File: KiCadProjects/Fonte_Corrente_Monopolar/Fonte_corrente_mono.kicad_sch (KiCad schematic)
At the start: 24 parts, among them J1 Vref, J2 tensoes, J3 sinais analogicos, J4 comunicacao / sinais digitais, J5 Vref, J6 Pinos de verificação, U1 AD828AN, U2 INA128, U3 AD828AN

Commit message: autosave backup
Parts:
- J1, J5: footprint (none) -> Connector_PinHeader_2.54mm:PinHeader_1x03_P2.54mm_Vertical
- U1, U3: footprint AD828:N_8_ADI -> AD828AN:N_8_ADI
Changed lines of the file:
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@@
       (effects (font (size 1.27 1.27)) (justify right))
     )
-    (property "Footprint" "" (at 229.87 95.885 0)
+    (property "Footprint" "Connector_PinHeader_2.54mm:PinHeader_1x03_P2.54mm_Vertical" (at 229.87 95.885 0)
       (effects (font (size 1.27 1.27)) hide)
     )
@@
       (effects (font (size 1.524 1.524)))
     )
-    (property "Footprint" "AD828:N_8_ADI" (at 118.745 116.84 0)
+    (property "Footprint" "AD828AN:N_8_ADI" (at 118.745 116.84 0)
       (effects (font (size 1.27 1.27) italic) hide)
     )
@@
       (effects (font (size 1.27 1.27)) (justify right))
     )
-    (property "Footprint" "" (at 177.8 95.885 0)
+    (property "Footprint" "Connector_PinHeader_2.54mm:PinHeader_1x03_P2.54mm_Vertical" (at 177.8 95.885 0)
       (effects (font (size 1.27 1.27)) hide)
     )
@@
       (effects (font (size 1.524 1.524)))
     )
-    (property "Footprint" "AD828:N_8_ADI" (at 58.674 33.274 0)
+    (property "Footprint" "AD828AN:N_8_ADI" (at 58.674 33.274 0)
       (effects (font (size 1.27 1.27) italic) hide)
     )

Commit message: alterações PCB
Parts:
- renumbered Rg1 to RganhoINA1, Rs1 to Rsentinela1
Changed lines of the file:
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@@
   (symbol (lib_id "Device:R") (at 195.58 45.72 0) (unit 1)
     (in_bom yes) (on_board yes) (dnp no) (fields_autoplaced)
-    (property "Reference" "Rg1" (at 198.12 45.085 0)
+    (property "Reference" "RganhoINA1" (at 198.12 44.45 0)
       (effects (font (size 1.27 1.27)) (justify left))
     )
-    (property "Value" "3,3k" (at 198.12 47.625 0)
+    (property "Value" "3,3k" (at 198.12 46.99 0)
       (effects (font (size 1.27 1.27)) (justify left))
     )
@@
       (project "Fonte_corrente_mono"
         (path "/f0ff92cf-26e5-4ab9-977d-5f9689e8a5d0"
-          (reference "Rg1") (unit 1)
+          (reference "RganhoINA1") (unit 1)
         )
       )
@@
   (symbol (lib_id "Device:R") (at 183.515 45.72 0) (unit 1)
     (in_bom yes) (on_board yes) (dnp no) (fields_autoplaced)
-    (property "Reference" "Rs1" (at 185.42 45.085 0)
+    (property "Reference" "Rsentinela1" (at 185.42 44.45 0)
       (effects (font (size 1.27 1.27)) (justify left))
     )
-    (property "Value" "10" (at 185.42 47.625 0)
+    (property "Value" "10" (at 185.42 46.99 0)
       (effects (font (size 1.27 1.27)) (justify left))
     )
@@
       (project "Fonte_corrente_mono"
         (path "/f0ff92cf-26e5-4ab9-977d-5f9689e8a5d0"
-          (reference "Rs1") (unit 1)
+          (reference "Rsentinela1") (unit 1)
         )
       )

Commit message: autosave backup
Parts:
- added SW_kcd1: sw, Chave_Gangorra:chave gangorra 3 pinos, symbol chave_gangorra_kcd1_2pinos:chave_gangorra_
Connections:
- net Sin1: now also SW_kcd1. (1a)
- net SinA: now also SW_kcd1. (1a)
- net switch_out_1: no longer names the net of U1.3 (+IN1)
- net switch_out_1: now also SW_kcd1. (1a)

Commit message: alterações PCB
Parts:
- removed J6: Pinos de verificação, Connector_PinHeader_2.54mm:PinHeader_1x14_P2.54mm_Horizontal, symbol Connector_Generic:Conn_01x14
- removed SW_kcd1: sw, Chave_Gangorra:chave gangorra 3 pinos, symbol chave_gangorra_kcd1_2pinos:chave_gangorra_
- added SW_kcd1: sw, Chave_Gangorra:chave gangorra 3 pinos, symbol chave_gangorra_kcd1:chave_gangorra_
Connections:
- net Sin1: now also SW_kcd1.2 (1a)
- net SinA: now also SW_kcd1.3 (1b)
- net at U1.3 (+IN1): now also SW_kcd1.1

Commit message: alterações PCB
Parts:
- renumbered U1 to U1-howland1, U3 to U3-cond1
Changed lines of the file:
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@@
   (symbol (lib_id "AD828AN:AD828AN") (at 118.745 116.84 0) (unit 1)
     (in_bom yes) (on_board yes) (dnp no) (fields_autoplaced)
-    (property "Reference" "U3" (at 139.065 107.95 0)
+    (property "Reference" "U3-cond1" (at 139.065 106.68 0)
       (effects (font (size 1.524 1.524)))
     )
-    (property "Value" "AD828AN" (at 139.065 110.49 0)
+    (property "Value" "AD828AN" (at 139.065 109.22 0)
       (effects (font (size 1.524 1.524)))
     )
@@
       (project "Fonte_corrente_mono"
         (path "/f0ff92cf-26e5-4ab9-977d-5f9689e8a5d0"
-          (reference "U3") (unit 1)
+          (reference "U3-cond1") (unit 1)
         )
       )
@@
   (symbol (lib_id "2023-04-18_19-29-20:AD828AN") (at 58.42 33.02 0) (unit 1)
     (in_bom yes) (on_board yes) (dnp no) (fields_autoplaced)
-    (property "Reference" "U1" (at 78.74 24.13 0)
+    (property "Reference" "U1-howland1" (at 78.74 22.86 0)
       (effects (font (size 1.524 1.524)))
     )
-    (property "Value" "AD828AN" (at 78.74 26.67 0)
+    (property "Value" "AD828AN" (at 78.74 25.4 0)
       (effects (font (size 1.524 1.524)))
     )
@@
       (project "Fonte_corrente_mono"
         (path "/f0ff92cf-26e5-4ab9-977d-5f9689e8a5d0"
-          (reference "U1") (unit 1)
-        )
-      )
+          (reference "U1-howland1") (unit 1)
+        )
+      )

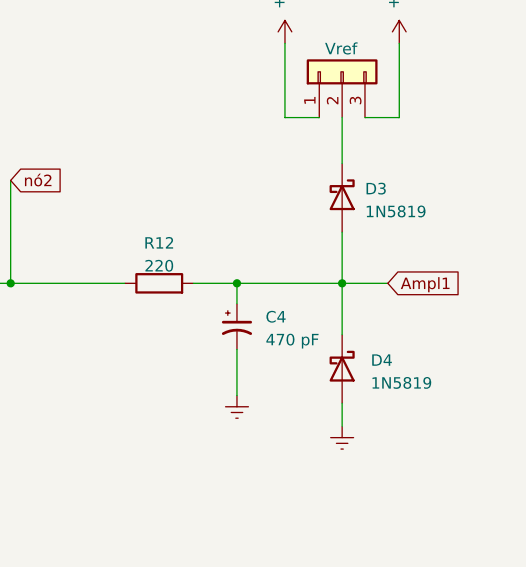
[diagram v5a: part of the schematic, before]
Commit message: alterações PCB: tamanho de pad
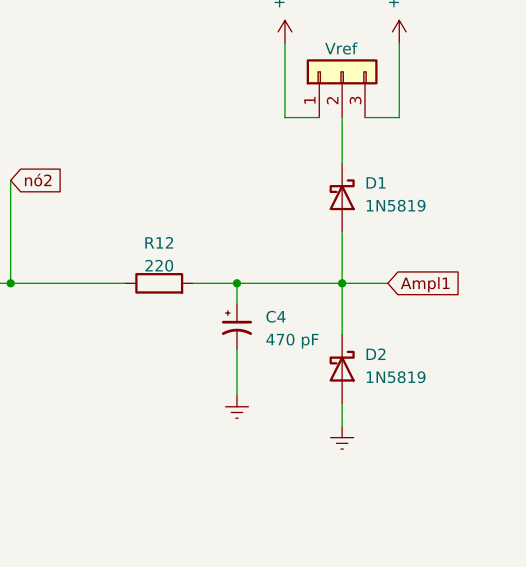
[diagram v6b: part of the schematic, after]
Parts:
- renumbered D3 to D1, D4 to D2
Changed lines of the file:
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@@
   (symbol (lib_id "Diode:1N5819") (at 229.87 109.855 270) (unit 1)
     (in_bom yes) (on_board yes) (dnp no) (fields_autoplaced)
-    (property "Reference" "D3" (at 232.41 108.9025 90)
+    (property "Reference" "D1" (at 232.41 108.2675 90)
       (effects (font (size 1.27 1.27)) (justify left))
     )
-    (property "Value" "1N5819" (at 232.41 111.4425 90)
+    (property "Value" "1N5819" (at 232.41 110.8075 90)
       (effects (font (size 1.27 1.27)) (justify left))
     )
@@
       (project "Fonte_corrente_mono"
         (path "/f0ff92cf-26e5-4ab9-977d-5f9689e8a5d0"
-          (reference "D3") (unit 1)
+          (reference "D1") (unit 1)
         )
       )
@@
   (symbol (lib_id "Diode:1N5819") (at 229.87 128.905 270) (unit 1)
     (in_bom yes) (on_board yes) (dnp no) (fields_autoplaced)
-    (property "Reference" "D4" (at 233.045 127.9525 90)
+    (property "Reference" "D2" (at 232.41 127.3175 90)
       (effects (font (size 1.27 1.27)) (justify left))
     )
-    (property "Value" "1N5819" (at 233.045 130.4925 90)
+    (property "Value" "1N5819" (at 232.41 129.8575 90)
       (effects (font (size 1.27 1.27)) (justify left))
     )
@@
       (project "Fonte_corrente_mono"
         (path "/f0ff92cf-26e5-4ab9-977d-5f9689e8a5d0"
-          (reference "D4") (unit 1)
+          (reference "D2") (unit 1)
         )
       )

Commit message: alterações PCB
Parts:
- removed J5: Vref, Connector_PinHeader_2.54mm:PinHeader_1x03_P2.54mm_Vertical, symbol Connector_Generic:Conn_01x03
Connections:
- net at D1.1 (K): now also J1.2 (Pin_2), R10.1
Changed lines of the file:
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@@
   (junction (at 159.385 119.38) (diameter 0) (color 0 0 0 0)
   )
+  (junction (at 177.8 102.87) (diameter 0) (color 0 0 0 0)
+  )
   (junction (at 177.8 119.38) (diameter 0) (color 0 0 0 0)
   )
@@
   (junction (at 108.585 35.56) (diameter 0) (color 0 0 0 0)
   )
-  (wire (pts (xy 227.33 100.965) (xy 223.52 100.965))
-    (stroke (width 0) (type default))
-  )
   (wire (pts (xy 172.085 181.61) (xy 172.085 187.325))
     (stroke (width 0) (type default))
@@
     (stroke (width 0) (type default))
   )
+  (wire (pts (xy 177.8 102.87) (xy 229.87 102.87))
+    (stroke (width 0) (type default))
+  )
   (wire (pts (xy 120.65 35.56) (xy 120.65 44.196))
     (stroke (width 0) (type default))
@@
     (stroke (width 0) (type default))
   )
+  (wire (pts (xy 229.87 102.87) (xy 229.87 106.045))
+    (stroke (width 0) (type default))
+  )
   (wire (pts (xy 165.1 119.38) (xy 170.18 119.38))
     (stroke (width 0) (type default))
@@
     (stroke (width 0) (type default))
   )
-  (wire (pts (xy 236.22 100.965) (xy 236.22 92.71))
-    (stroke (width 0) (type default))
-  )
   (wire (pts (xy 118.745 68.58) (xy 120.65 68.58))
     (stroke (width 0) (type default))
@@
     (stroke (width 0) (type default))
   )
-  (wire (pts (xy 223.52 100.965) (xy 223.52 92.71))
-    (stroke (width 0) (type default))
-  )
   (wire (pts (xy 184.785 100.965) (xy 184.785 92.71))
     (stroke (width 0) (type default))
@@
     (stroke (width 0) (type default))
   )
-  (wire (pts (xy 232.41 100.965) (xy 236.22 100.965))
-    (stroke (width 0) (type default))
-  )
   (wire (pts (xy 174.625 181.61) (xy 174.625 187.325))
     (stroke (width 0) (type default))
@@
     (stroke (width 0) (type default))
   )
-  (wire (pts (xy 177.8 104.14) (xy 177.8 100.965))
+  (wire (pts (xy 177.8 104.14) (xy 177.8 102.87))
     (stroke (width 0) (type default))
   )
@@
     (stroke (width 0) (type default))
   )
+  (wire (pts (xy 177.8 102.87) (xy 177.8 100.965))
+    (stroke (width 0) (type default))
+  )
   (wire (pts (xy 99.06 40.64) (xy 99.06 68.58))
     (stroke (width 0) (type default))
@@
   )
   (wire (pts (xy 159.766 116.84) (xy 159.385 116.84))
-    (stroke (width 0) (type default))
-  )
-  (wire (pts (xy 229.87 100.965) (xy 229.87 106.045))
     (stroke (width 0) (type default))
   )
@@
     )
   )
-  (symbol (lib_id "Connector_Generic:Conn_01x03") (at 229.87 95.885 90) (unit 1)
-    (in_bom yes) (on_board yes) (dnp no)
-    (property "Reference" "J5" (at 224.155 97.155 90)
-      (effects (font (size 1.27 1.27)) (justify left) hide)
-    )
-    (property "Value" "Vref" (at 227.965 93.345 90)
-      (effects (font (size 1.27 1.27)) (justify right))
-    )
-    (property "Footprint" "Connector_PinHeader_2.54mm:PinHeader_1x03_P2.54mm_Vertical" (at 229.87 95.885 0)
-      (effects (font (size 1.27 1.27)) hide)
-    )
-    (property "Datasheet" "~" (at 229.87 95.885 0)
-      (effects (font (size 1.27 1.27)) hide)
-    )
-    (pin "1")
-    (pin "2")
-    (pin "3")
-    (instances
-      (project "Fonte_corrente_mono"
-        (path "/f0ff92cf-26e5-4ab9-977d-5f9689e8a5d0"
-          (reference "J5") (unit 1)
-        )
-      )
-    )
-  )
   (symbol (lib_id "power:VCC") (at 31.242 187.96 0) (unit 1)
     (in_bom yes) (on_board yes) (dnp no)
@@
         (path "/f0ff92cf-26e5-4ab9-977d-5f9689e8a5d0"
           (reference "#PWR02") (unit 1)
-        )
-      )
-    )
-  )
-  (symbol (lib_id "power:+5V") (at 236.22 92.71 0) (unit 1)
-    (in_bom yes) (on_board yes) (dnp no) (fields_autoplaced)
-    (property "Reference" "#PWR012" (at 236.22 96.52 0)
-      (effects (font (size 1.27 1.27)) hide)
-    )
-    (property "Value" "+5V" (at 235.585 88.9 90)
-      (effects (font (size 1.27 1.27)) (justify left))
-    )
-    (property "Footprint" "" (at 236.22 92.71 0)
-      (effects (font (size 1.27 1.27)) hide)
-    )
-    (property "Datasheet" "" (at 236.22 92.71 0)
-      (effects (font (size 1.27 1.27)) hide)
-    )
-    (pin "1")
-    (instances
-      (project "Fonte_corrente_mono"
-        (path "/f0ff92cf-26e5-4ab9-977d-5f9689e8a5d0"
-          (reference "#PWR012") (unit 1)
         )
       )
@@
         )
       )
-    )
-  )
-  (symbol (lib_id "power:+3.3V") (at 223.52 92.71 0) (unit 1)
-    (in_bom yes) (on_board yes) (dnp no) (fields_autoplaced)
-    (property "Reference" "#PWR010" (at 223.52 96.52 0)
-      (effects (font (size 1.27 1.27)) hide)
-    )
-    (property "Value" "+3.3V" (at 222.885 88.9 90)
-      (effects (font (size 1.27 1.27)) (justify left))
-    )
-    (property "Footprint" "" (at 223.52 92.71 0)
-      (effects (font (size 1.27 1.27)) hide)
-    )
-    (property "Datasheet" "" (at 223.52 92.71 0)
-      (effects (font (size 1.27 1.27)) hide)
-    )
-    (pin "1")
-    (instances
-      (project "Fonte_corrente_mono"
-        (path "/f0ff92cf-26e5-4ab9-977d-5f9689e8a5d0"
-          (reference "#PWR010") (unit 1)
-        )
-      )
